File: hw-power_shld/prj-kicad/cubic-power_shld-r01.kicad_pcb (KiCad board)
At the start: 2 copper layers, 13.3 x 24.5 mm, 17 parts

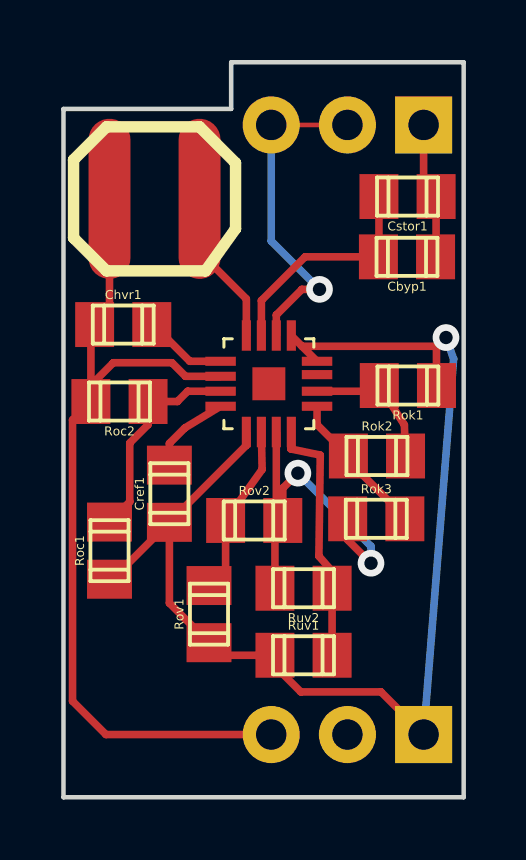
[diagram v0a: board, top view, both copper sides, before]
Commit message: add GND plan.
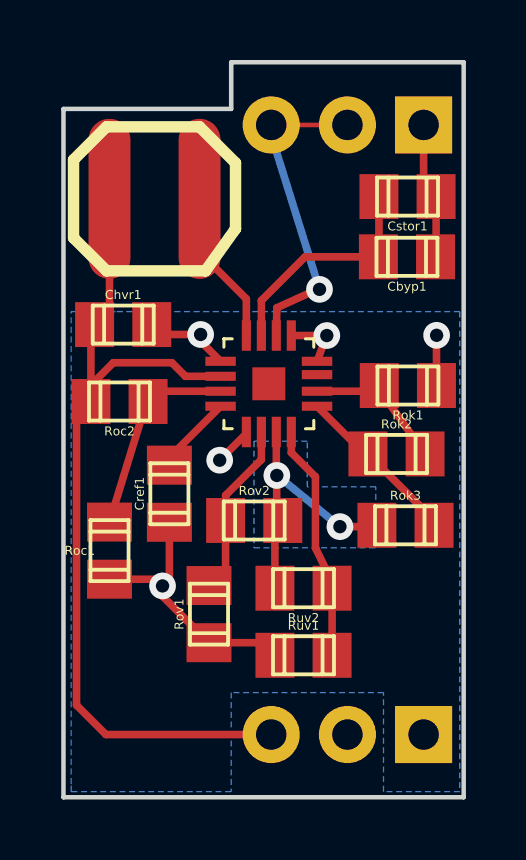
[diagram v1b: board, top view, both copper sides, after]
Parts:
- moved Rok3 1.00 mm to (180.3, 90.4)
- moved Rok2 0.66 mm to (180.0, 88.1)
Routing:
- net GND: track 44.0 -> 17.9 mm, vias 1 -> 5
- net N-000006: track 13.0 -> 9.21 mm
- net N-000004: track 4.96 -> 5.64 mm
- added copper zone on B.Cu, net GND
